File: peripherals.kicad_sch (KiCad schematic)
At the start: 29 parts, among them U1 MIMX8MM6DVTLZAA, U32 74LVC1G07, U33 74LVC1G07

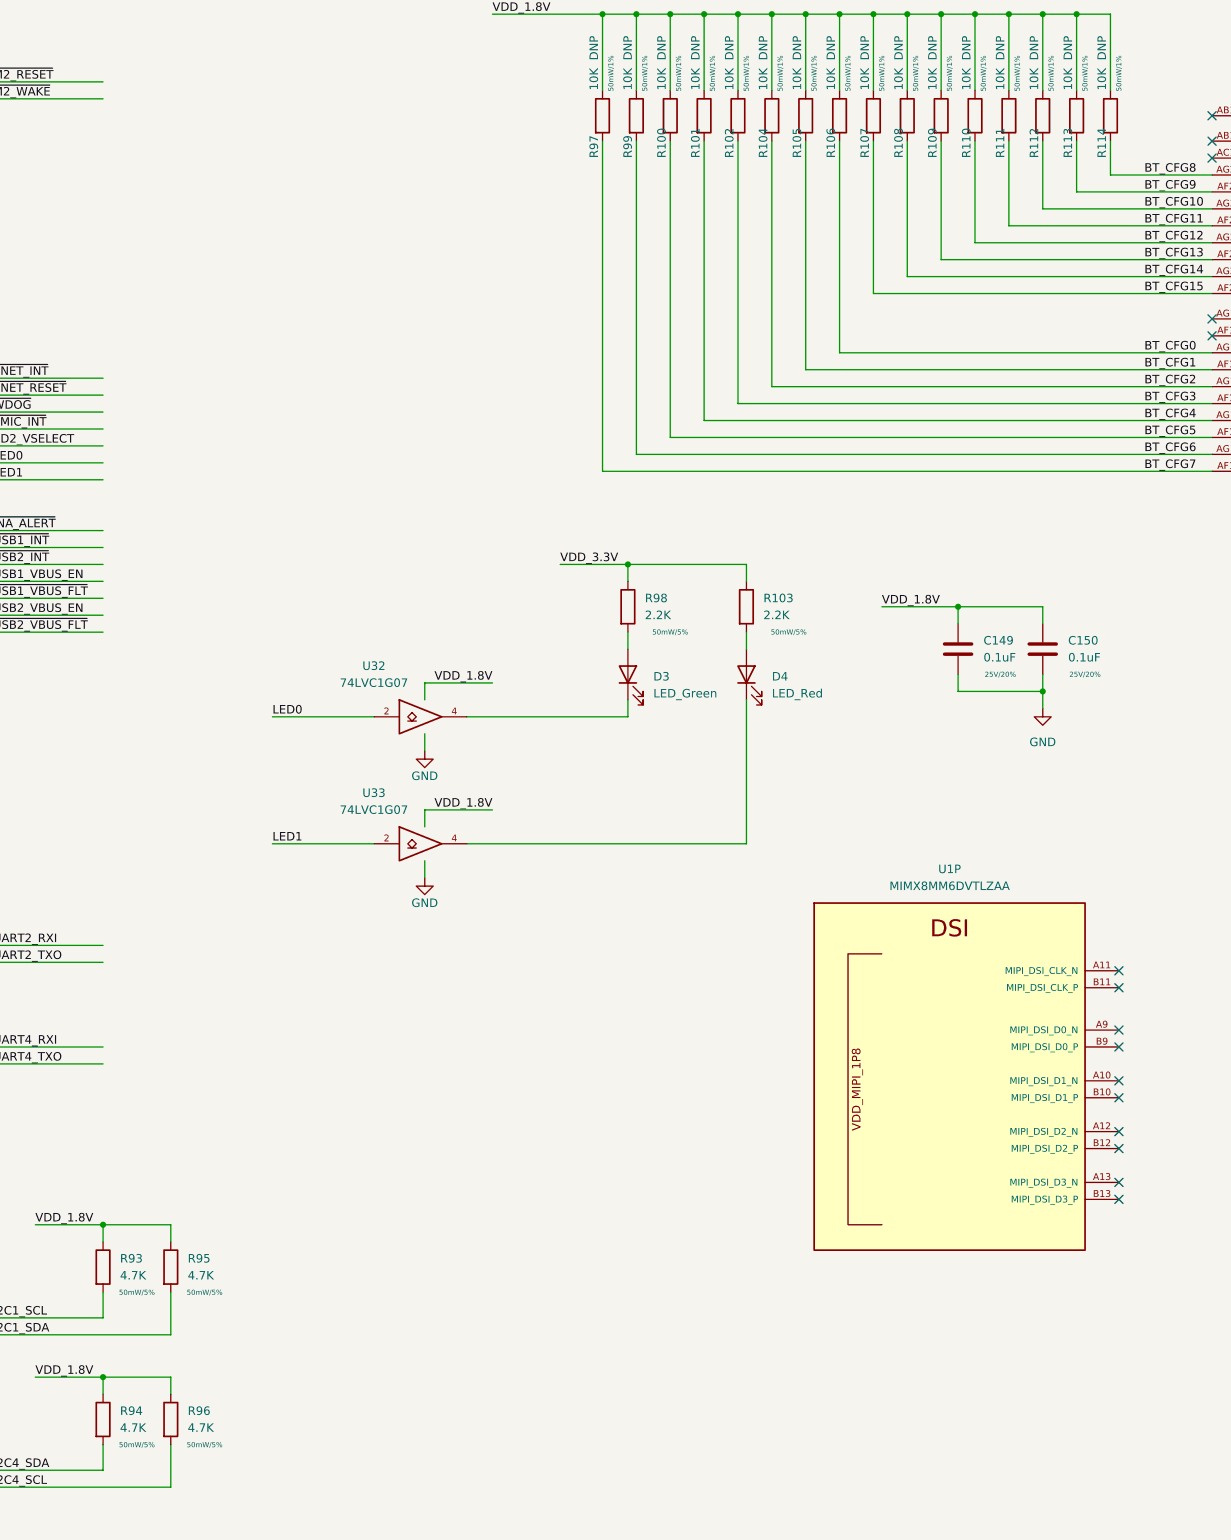
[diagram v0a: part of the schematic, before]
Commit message: v2 of ddr flytimes tool, lots of routing work, sch fixes
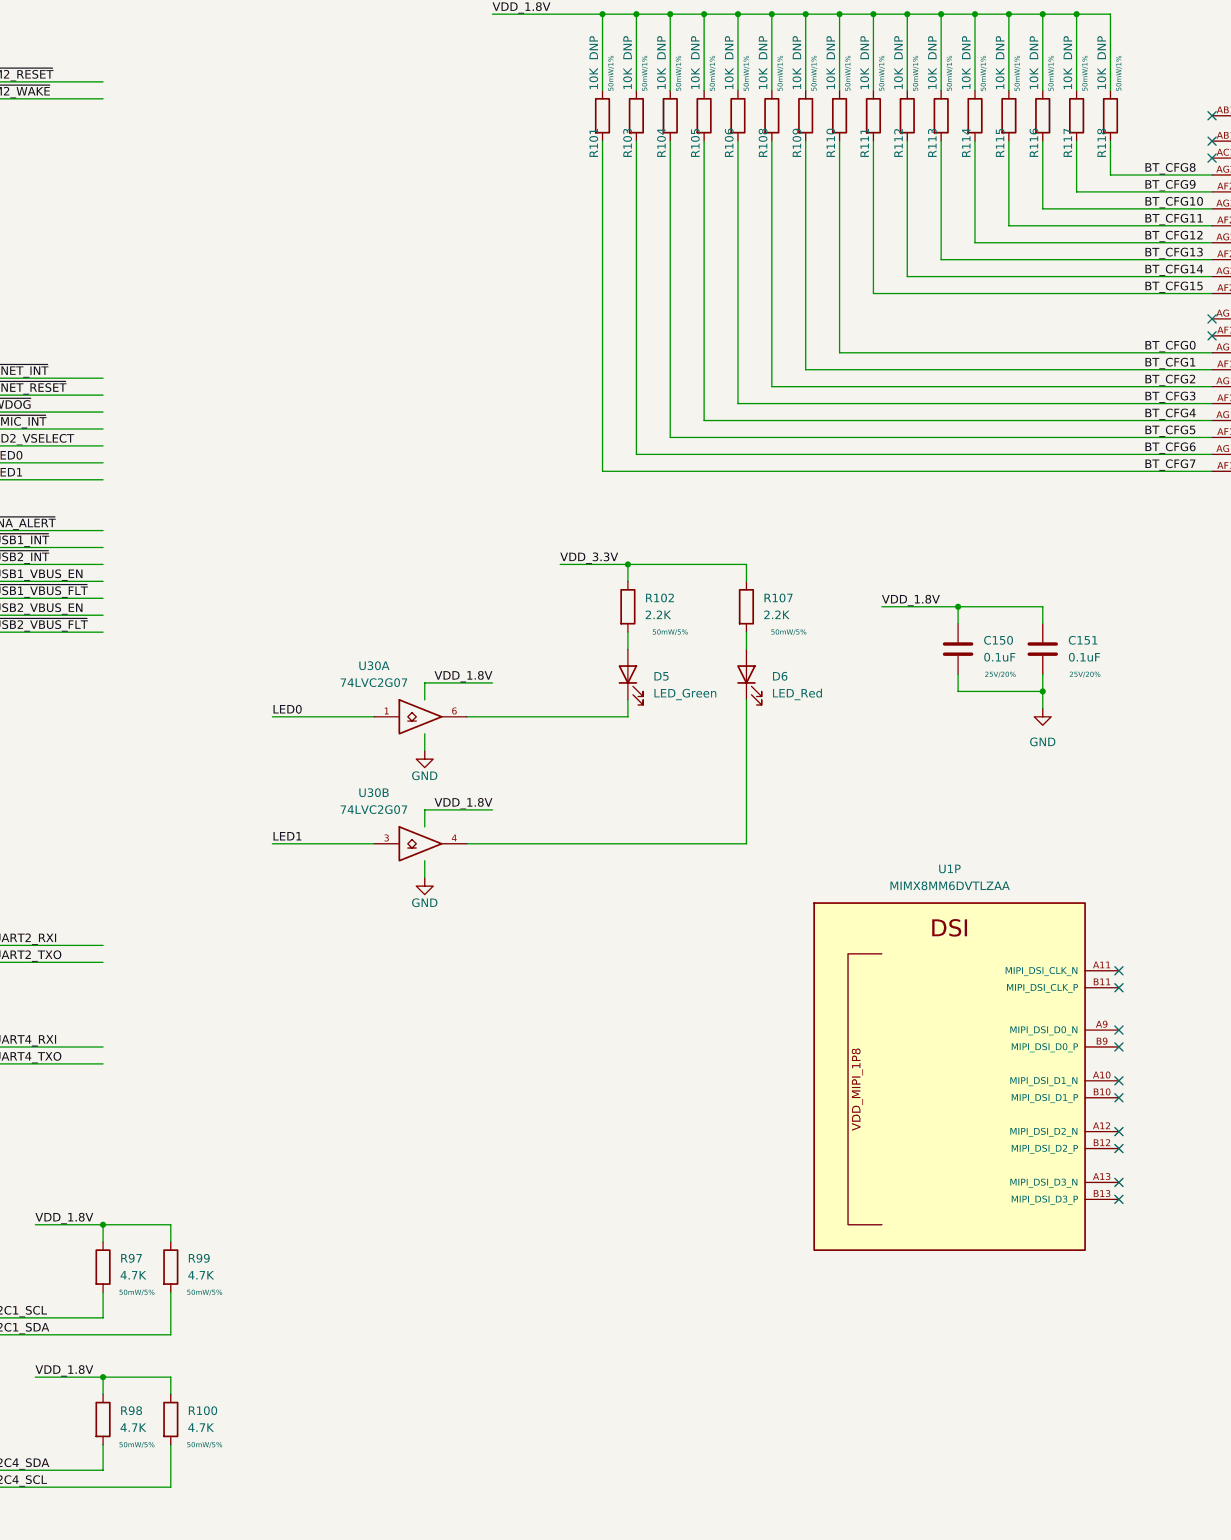
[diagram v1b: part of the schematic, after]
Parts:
- removed U32, U33: 74LVC1G07, Package_TO_SOT_SMD:SOT-23-5, symbol 74xGxx:74LVC1G07
- added U30: 74LVC2G07, Package_TO_SOT_SMD:SOT-886, symbol 74xGxx:74LVC2G07
- renumbered C149 to C150, C150 to C151, D3 to D5, D4 to D6, R96 to R100, R97 to R101, R98 to R102, R99 to R103, R100 to R104, R101 to R105, R102 to R106, R103 to R107, R104 to R108, R105 to R109, R106 to R110, R107 to R111, R108 to R112, R109 to R113, R110 to R114, R111 to R115, R112 to R116, R113 to R117, R114 to R118, R93 to R97, R94 to R98, R95 to R99
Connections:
- net GND: now also U30.2 (GND), U30.2 (GND)
- net LED0: now also U30.1
- net LED1: now also U30.3
- net VCC: now also U30.5 (VCC), U30.5 (VCC)
- net at D6.1 (K): now also U30.4
- net at D5.1 (K): now also U30.6

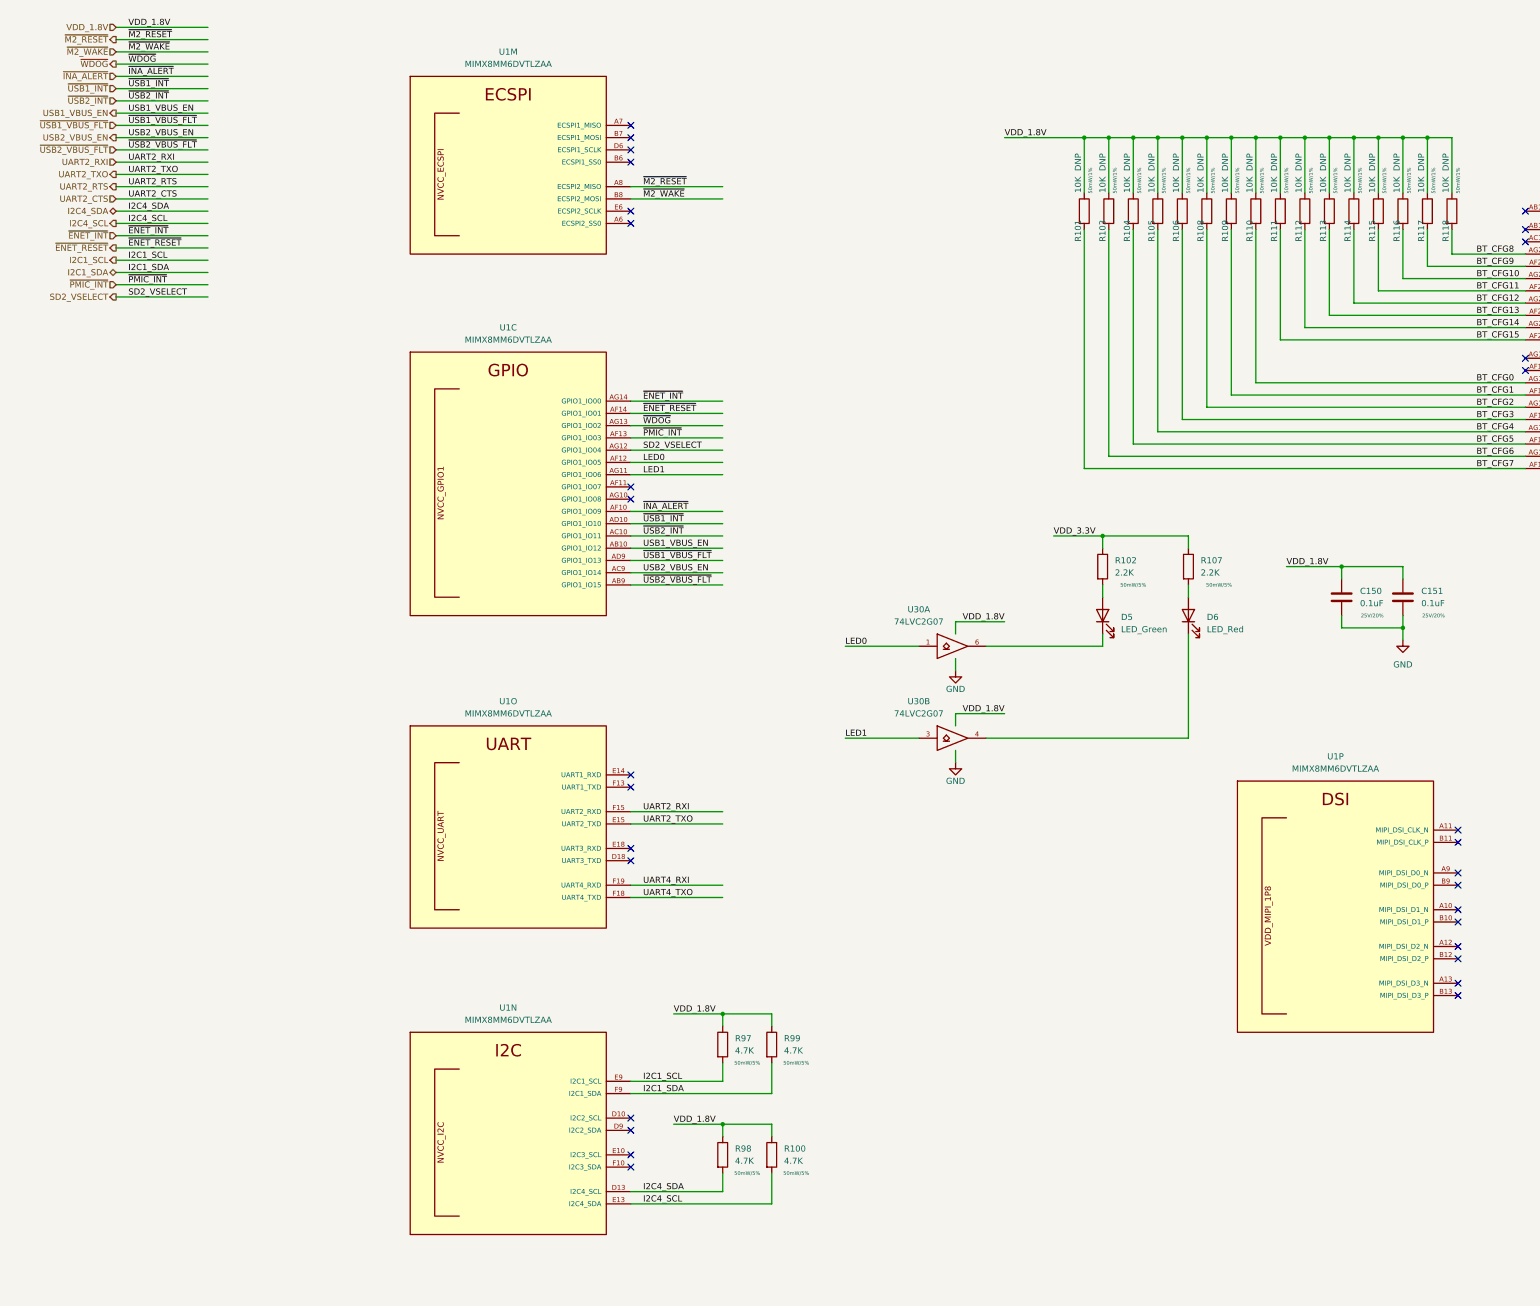
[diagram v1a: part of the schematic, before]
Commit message: more routing work, prepare to change to x32 lpddr4
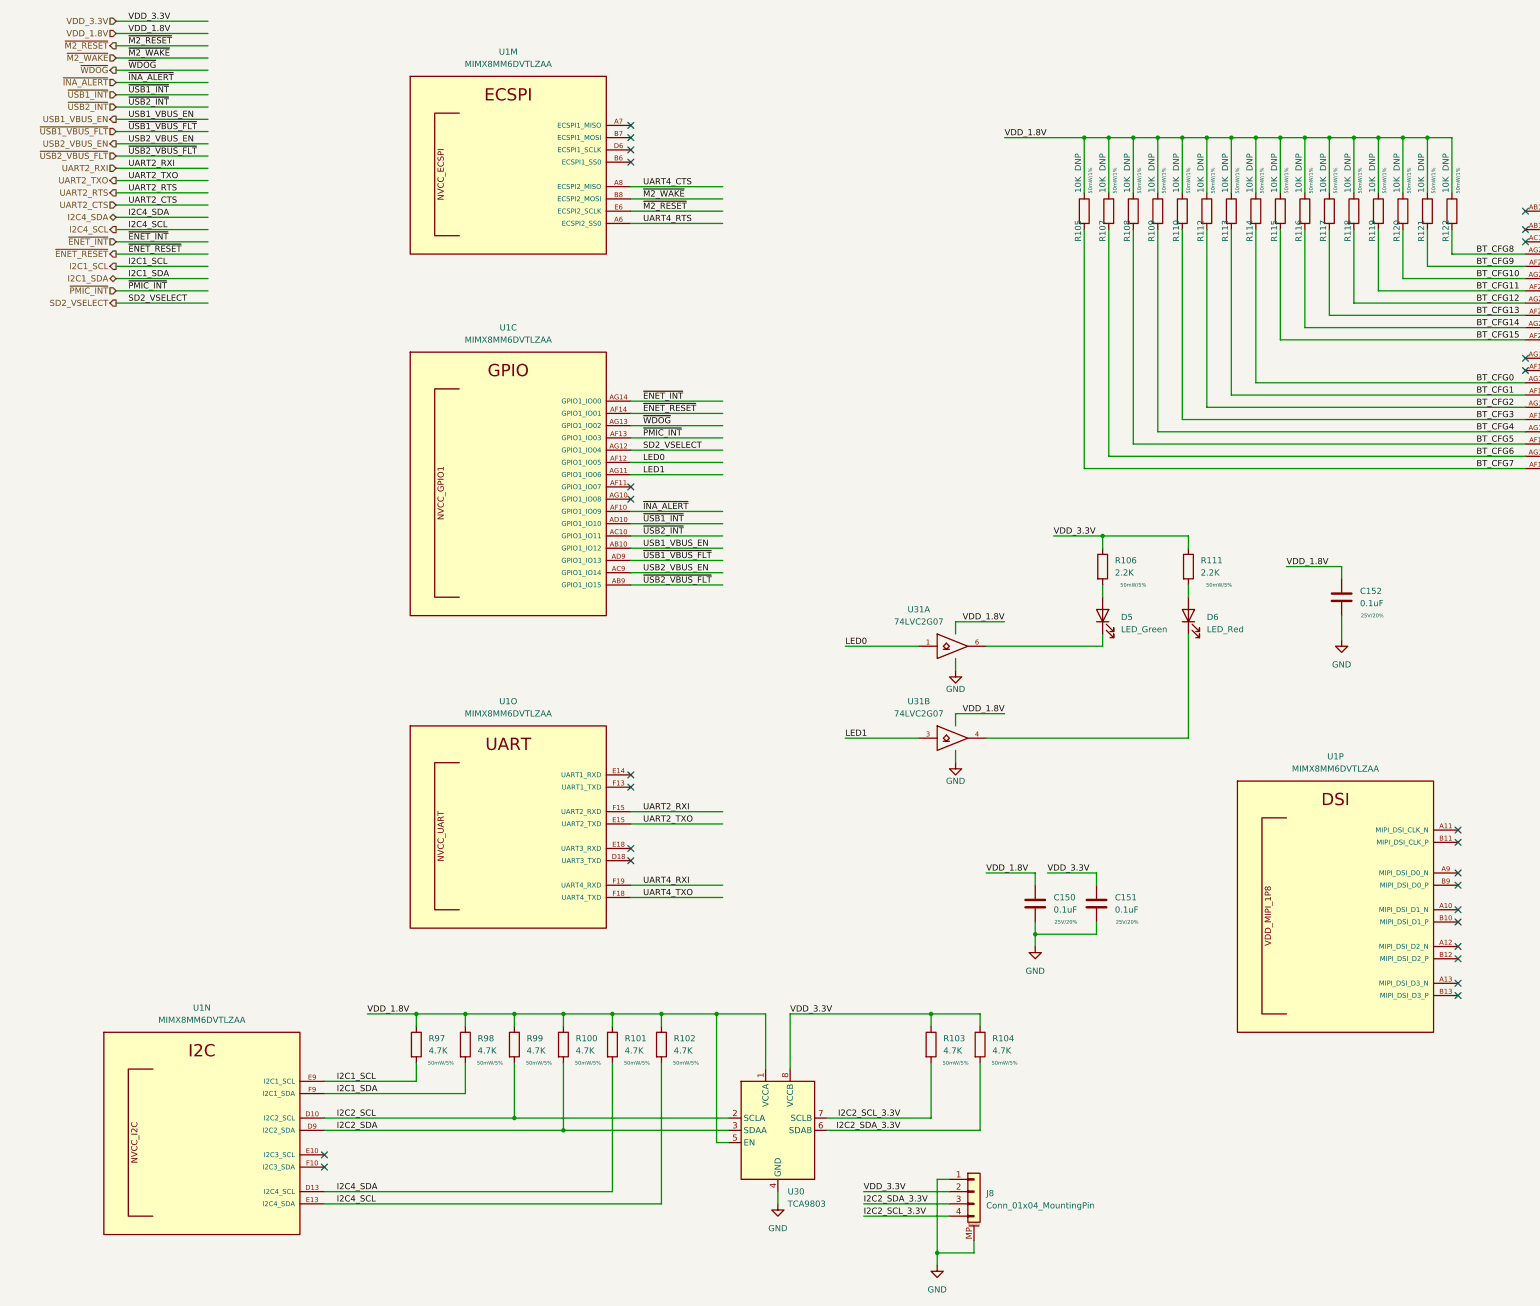
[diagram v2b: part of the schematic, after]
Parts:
- added C150: 0.1uF, Capacitor_SMD:C_0402_1005Metric, symbol Device:C
- added J8: Conn_01x04_MountingPin, Connector_JST:JST_SH_SM04B-SRSS-TB_1x04-1MP_P1.00mm_Horizontal, symbol Connector_Generic_MountingPin:Conn_01x04_MountingPin
- added R101, R102, R103, R104: 4.7K, Resistor_SMD:R_0402_1005Metric, symbol Device:R
- added U30: TCA9803, Package_SO:VSSOP-8_3.0x3.0mm_P0.65mm, symbol Interface:TCA9803
- renumbered C150 to C152, R101 to R105, R102 to R106, R103 to R107, R104 to R108, R105 to R109, R106 to R110, R107 to R111, R108 to R112, R109 to R113, R110 to R114, R111 to R115, R112 to R116, R113 to R117, R114 to R118, R115 to R119, R116 to R120, R117 to R121, R118 to R122, R99 to R98, R98 to R99, U30 to U31
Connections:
- net GND: now also C150.2, J8.1 (Pin_1), J8.MP (MountPin), U30.4 (GND)
- net I2C4_SCL: now also R102.2; no longer R100.2
- net I2C4_SDA: now also R101.2; no longer R99.2
- net VCC: now also C150.1, R101.1, R102.1, U30.1 (VCCA), U30.5 (EN); no longer C151.1
- net VDD_3.3V: now also C151.1, J8.2 (Pin_2), R103.1, R104.1, U30.8 (VCCB)
- net ~{M2_RESET}: now also U1.E6 (ECSPI2_SCLK); no longer U1.A8 (ECSPI2_MISO)
- net UART4_RTS: now reaches U1.A6 (ECSPI2_SS0)
- net I2C2_SCL: now reaches U1.D10 (I2C2_SCL)
- net I2C2_SCL: now also R99.2, U30.2 (SCLA)
- net I2C2_SDA: now reaches U1.D9 (I2C2_SDA)
- net I2C2_SDA: now also R100.2, U30.3 (SDAA)
- new net I2C2_SCL_3.3V: J8.4 (Pin_4), R103.2, U30.7 (SCLB)
- new net I2C2_SDA_3.3V: J8.3 (Pin_3), R104.2, U30.6 (SDAB)
- new net UART4_CTS: U1.A8 (ECSPI2_MISO)
- no-connect marks 53 -> 49
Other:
- moved on the sheet: R100, R97, R98, R99, U1N
